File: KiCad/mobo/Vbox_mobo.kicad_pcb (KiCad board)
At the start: 2 copper layers, 33.1 x 114.3 mm, 46 parts, among them J1 Conn_01x02, J10 Conn_01x01, J11 Conn_01x01, J12 Conn_01x02, J13 Conn_01x02, J14 Conn_01x02, J15 Conn_01x02, J2 JTAG_TC2030, J3 DuPont Connector, J4 Conn_01x06, J5 Conn_01x06, J6 Conn_01x10, J7 Conn_01x10, J8 Conn_01x01, J9 Conn_01x01, SW1 Boot, U1 XC6206, U2 X05A26H12G, U3 RP2040, U4 W25Q128JVS, Y1 12MHz

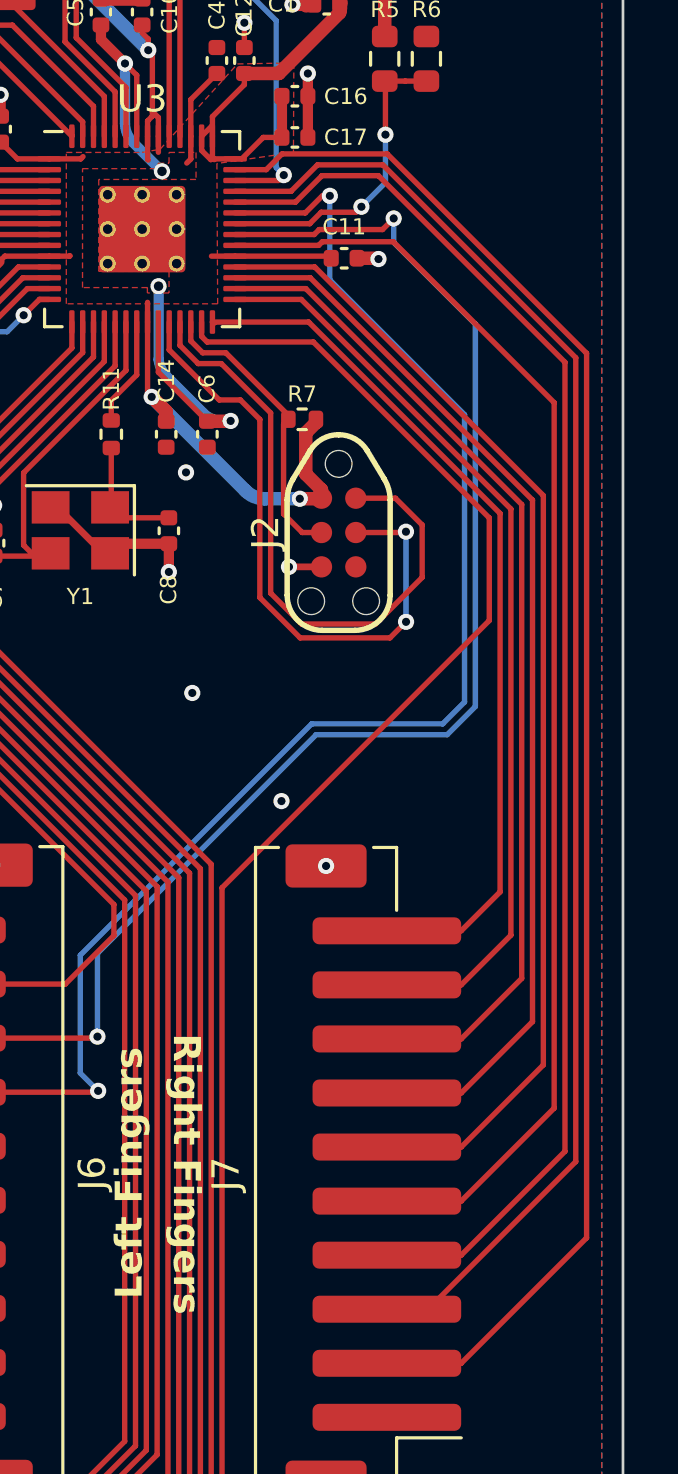
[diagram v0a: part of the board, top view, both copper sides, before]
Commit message: fix ugly track on mobo
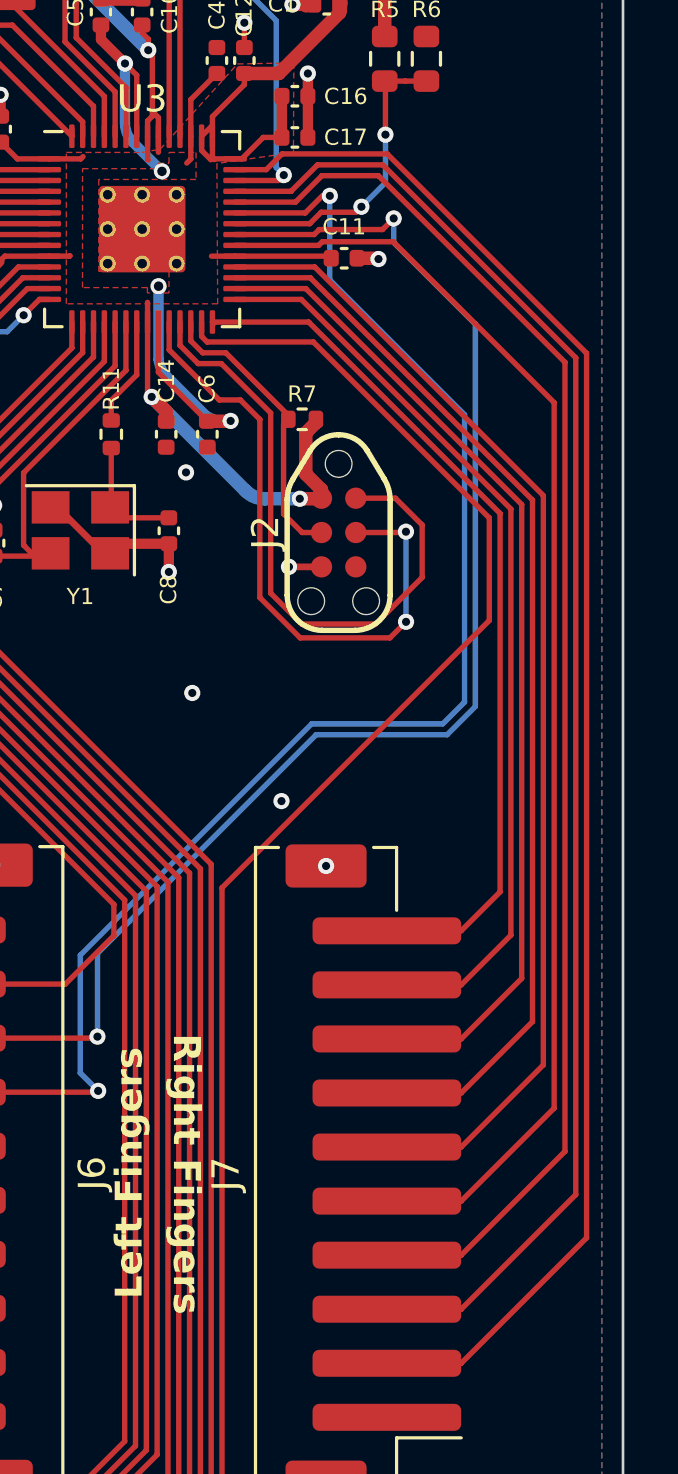
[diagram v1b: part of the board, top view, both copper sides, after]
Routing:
- net R: track 55.0 -> 55.7 mm
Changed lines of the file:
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@@
   (segment (start 115.9892 114.960801) (end 115.9892 85.7632) (width 0.2) (layer "F.Cu") (net 46))
   (segment (start 115.9892 85.7632) (end 109.0866 78.8606) (width 0.2) (layer "F.Cu") (net 46))
-  (segment (start 110.927818 120.800001) (end 116.3892 115.338619) (width 0.2) (layer "F.Cu") (net 47))
-  (segment (start 105.8546 79.438401) (end 106.8324 78.460601) (width 0.2) (layer "F.Cu") (net 47))
-  (segment (start 116.3892 115.338619) (end 116.3892 85.597515) (width 0.2) (layer "F.Cu") (net 47))
-  (segment (start 103.7831 79.438401) (end 105.8546 79.438401) (width 0.2) (layer "F.Cu") (net 47))
-  (segment (start 109.4 120.800001) (end 110.927818 120.800001) (width 0.2) (layer "F.Cu") (net 47))
-  (segment (start 106.8324 78.460601) (end 109.252286 78.460601) (width 0.2) (layer "F.Cu") (net 47))
-  (segment (start 109.252286 78.460601) (end 116.3892 85.597515) (width 0.2) (layer "F.Cu") (net 47))
+  (segment (start 109.4 120.800001) (end 112.149999 120.800001) (width 0.2) (layer "F.Cu") (net 47))
+  (segment (start 109.252286 78.460601) (end 106.8324 78.460601) (width 0.2) (layer "F.Cu") (net 47))
+  (segment (start 105.8546 79.438401) (end 103.7831 79.438401) (width 0.2) (layer "F.Cu") (net 47))
+  (segment (start 116.3892 85.597515) (end 109.252286 78.460601) (width 0.2) (layer "F.Cu") (net 47))
+  (segment (start 112.149999 120.800001) (end 116.3892 116.5608) (width 0.2) (layer "F.Cu") (net 47))
+  (segment (start 116.3892 116.5608) (end 116.3892 85.597515) (width 0.2) (layer "F.Cu") (net 47))
+  (segment (start 106.8324 78.460601) (end 105.8546 79.438401) (width 0.2) (layer "F.Cu") (net 47))
   (segment (start 97.906515 73.755096) (end 97.906516 71.230331) (width 0.2) (layer "F.Cu") (net 48))
   (segment (start 97.906516 71.230331) (end 96.570188 69.894003) (width 0.2) (layer "F.Cu") (net 48))

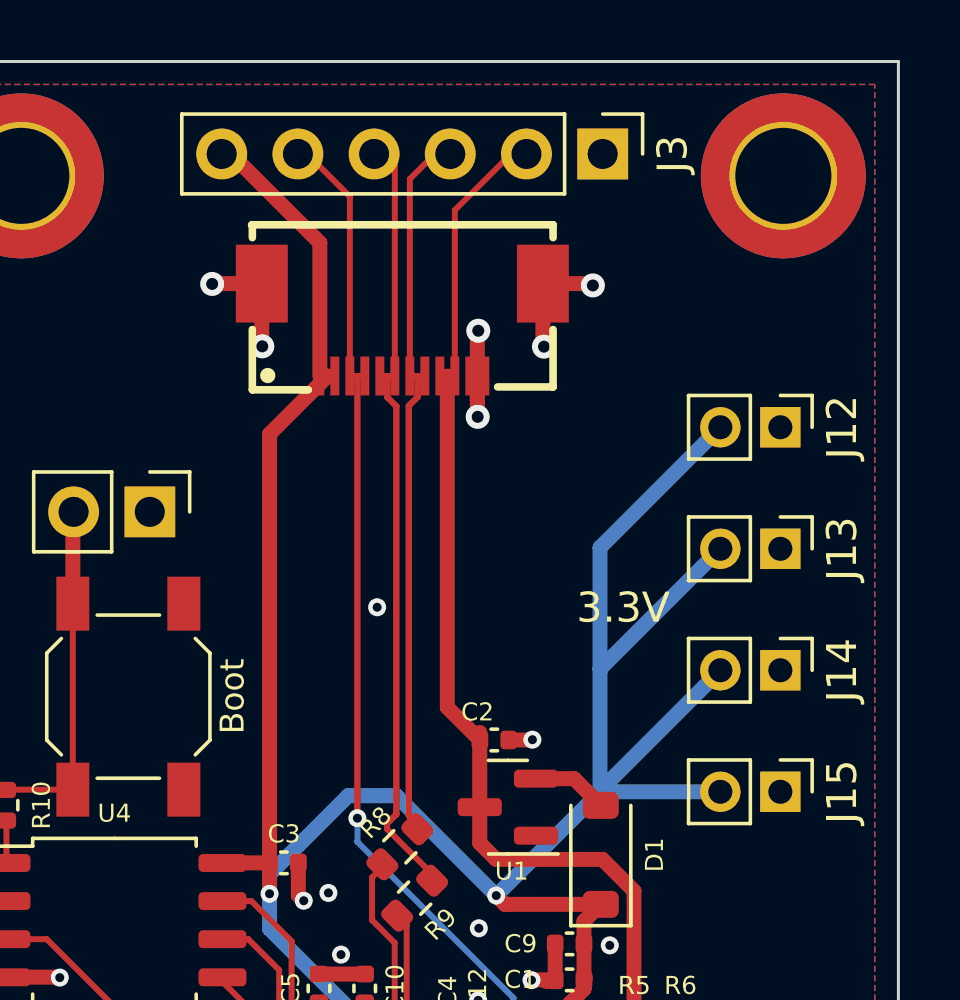
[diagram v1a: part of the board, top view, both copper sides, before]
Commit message: make mobo pads hand-solderable
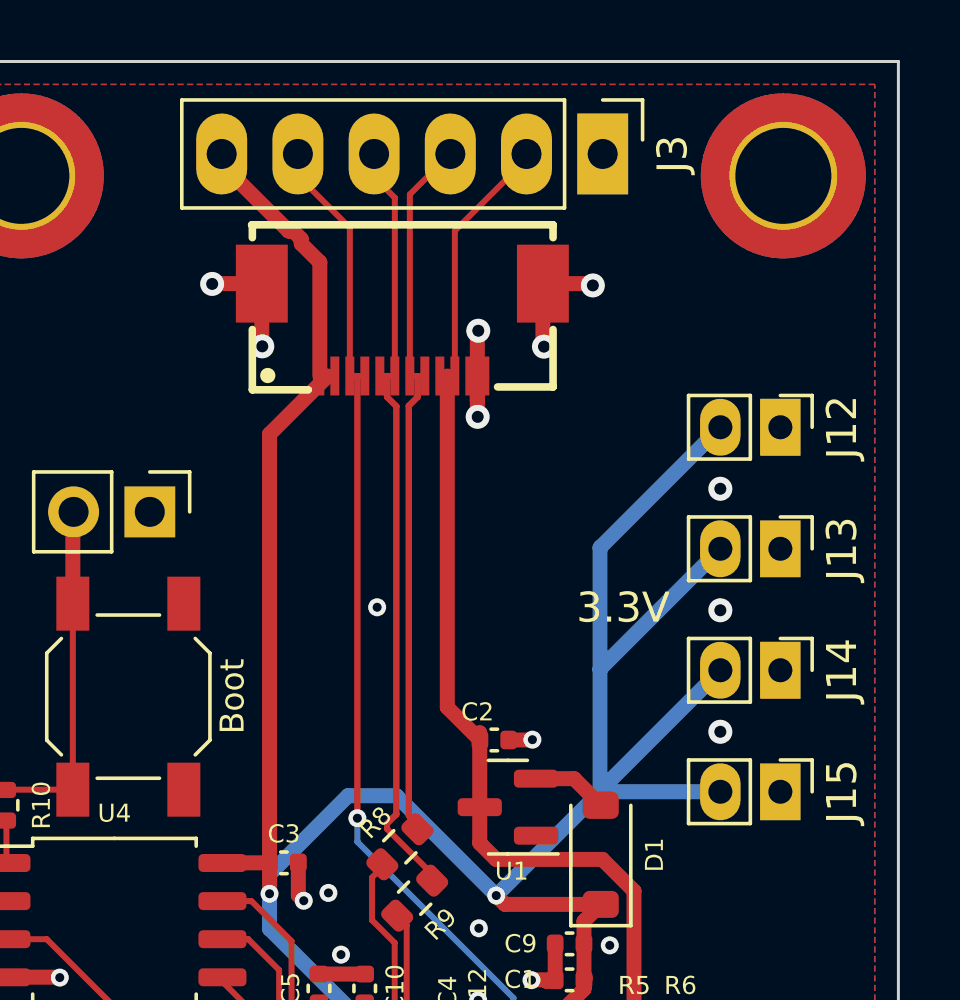
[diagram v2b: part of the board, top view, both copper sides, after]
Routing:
- net GND: vias 35 -> 38

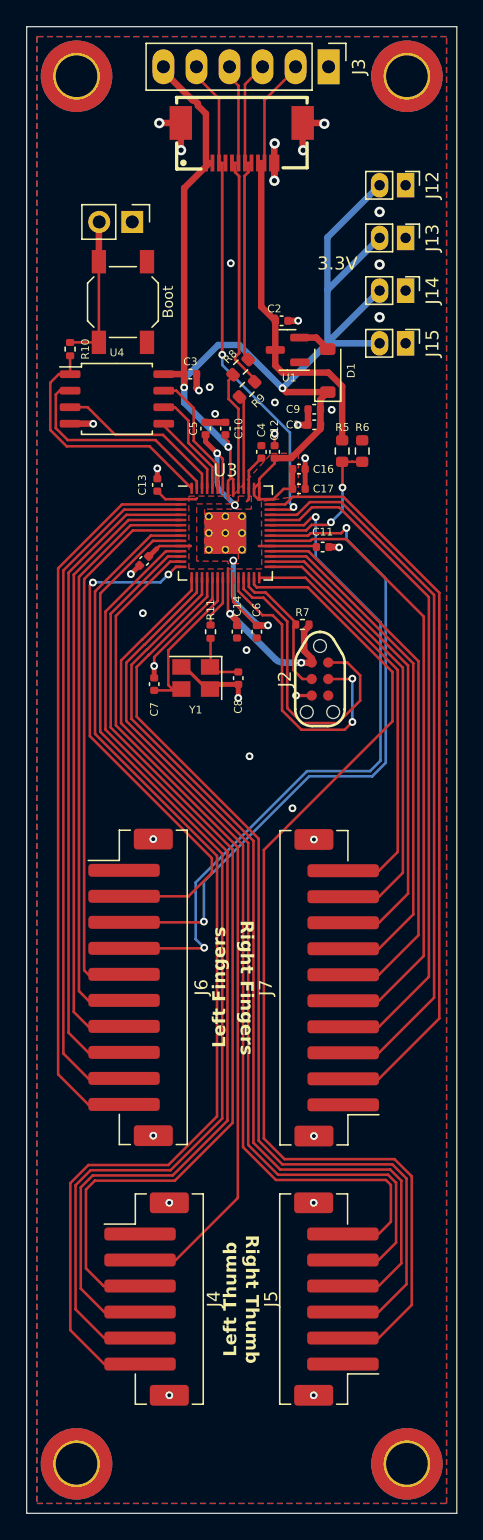
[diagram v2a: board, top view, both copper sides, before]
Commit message: adjust finger ergo, pullup resistors on mobo
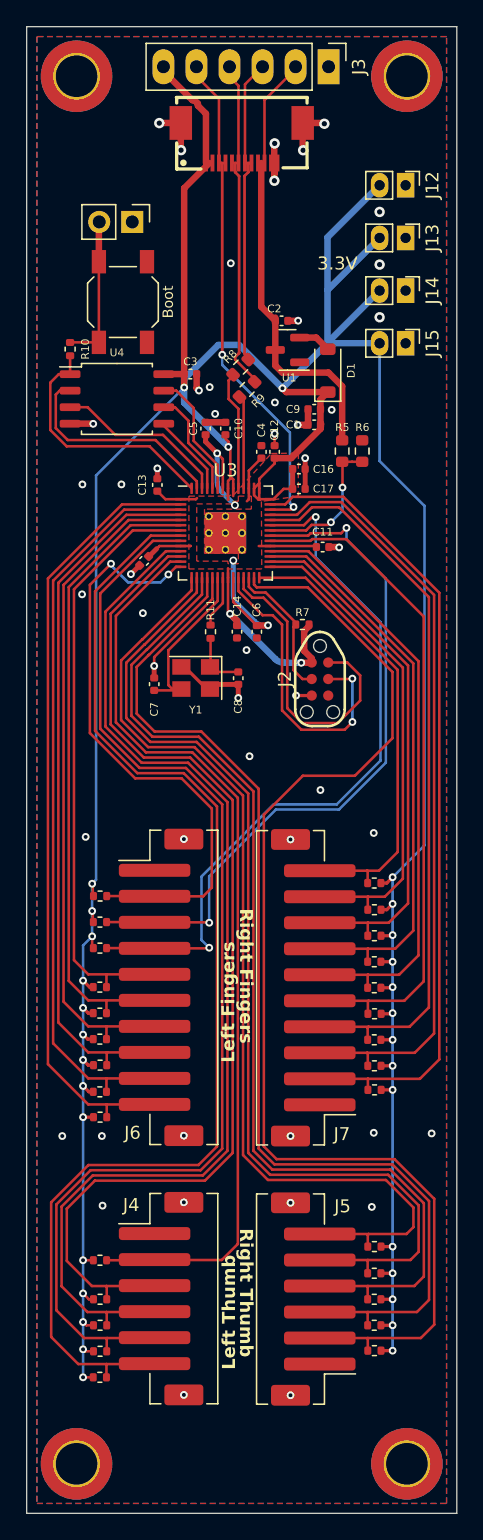
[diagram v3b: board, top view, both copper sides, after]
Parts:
- added R1: 2k, Resistor_SMD:R_0402_1005Metric, F.Cu at (90.7, 112.8)
- added R12: 2k, Resistor_SMD:R_0402_1005Metric, F.Cu at (90.7, 123.8)
- added R13: 2k, Resistor_SMD:R_0402_1005Metric, F.Cu at (90.7, 119.8)
- added R14: 2k, Resistor_SMD:R_0402_1005Metric, F.Cu at (90.7, 108.8)
- added R15: 2k, Resistor_SMD:R_0402_1005Metric, F.Cu at (90.7, 121.8)
- added R16: 2k, Resistor_SMD:R_0402_1005Metric, F.Cu at (90.7, 125.8)
- added R17: 2k, Resistor_SMD:R_0402_1005Metric, F.Cu at (111.8, 123.7)
- added R18: 2k, Resistor_SMD:R_0402_1005Metric, F.Cu at (111.8, 121.8)
- added R19: 2k, Resistor_SMD:R_0402_1005Metric, F.Cu at (111.8, 119.8)
- added R2: 2k, Resistor_SMD:R_0402_1005Metric, F.Cu at (90.7, 115.8)
- added R20: 2k, Resistor_SMD:R_0402_1005Metric, F.Cu at (111.8, 117.8)
- added R21: 2k, Resistor_SMD:R_0402_1005Metric, F.Cu at (111.8, 115.8)
- added R22: 2k, Resistor_SMD:R_0402_1005Metric, F.Cu at (111.8, 113.8)
- added R23: 2k, Resistor_SMD:R_0402_1005Metric, F.Cu at (111.8, 111.8)
- added R24: 2k, Resistor_SMD:R_0402_1005Metric, F.Cu at (111.8, 109.8)
- added R25: 2k, Resistor_SMD:R_0402_1005Metric, F.Cu at (111.8, 107.8)
- added R26: 2k, Resistor_SMD:R_0402_1005Metric, F.Cu at (90.7, 145.8)
- added R27: 2k, Resistor_SMD:R_0402_1005Metric, F.Cu at (90.7, 143.8)
- added R28: 2k, Resistor_SMD:R_0402_1005Metric, F.Cu at (90.7, 141.8)
- added R29: 2k, Resistor_SMD:R_0402_1005Metric, F.Cu at (90.7, 139.8)
- added R3: 2k, Resistor_SMD:R_0402_1005Metric, F.Cu at (90.7, 110.8)
- added R30: 2k, Resistor_SMD:R_0402_1005Metric, F.Cu at (90.7, 136.8)
- added R31: 2k, Resistor_SMD:R_0402_1005Metric, F.Cu at (111.8, 135.7)
- added R32: 2k, Resistor_SMD:R_0402_1005Metric, F.Cu at (111.8, 137.8)
- added R33: 2k, Resistor_SMD:R_0402_1005Metric, F.Cu at (111.8, 139.8)
- added R34: 2k, Resistor_SMD:R_0402_1005Metric, F.Cu at (111.8, 141.8)
- added R35: 2k, Resistor_SMD:R_0402_1005Metric, F.Cu at (111.8, 143.7)
- added R4: 2k, Resistor_SMD:R_0402_1005Metric, F.Cu at (90.7, 117.8)
- moved J6 2.35 mm to (95.4, 115.8)
- moved J7 1.80 mm to (107.1, 115.8)
- moved J5 1.78 mm to (107.1, 139.7)
- moved J4 1.12 mm to (95.4, 139.7)
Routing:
- net 3vDiode: track 135.3 -> 320.6 mm, vias 5 -> 33
- net M5: track 64.8 -> 72.7 mm
- net INDEX2: track 38.9 -> 46.6 mm
- net C_RT: track 82.7 -> 89.7 mm
- net M1: track 83.8 -> 90.6 mm
- net C_DN: track 75.9 -> 82.5 mm
- net M2: track 80.9 -> 87.5 mm
- net A: track 73.7 -> 80.2 mm
- net M3: track 77.2 -> 83.7 mm
- net C_LT: track 71.6 -> 77.9 mm
- net M4: track 74.4 -> 80.6 mm
- net C_UP: track 69.4 -> 75.5 mm
- net RING2: track 50.2 -> 54.2 mm
- net PINKY2: track 51.9 -> 55.8 mm
- net RIGHTSTART: track 58.3 -> 61.0 mm
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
